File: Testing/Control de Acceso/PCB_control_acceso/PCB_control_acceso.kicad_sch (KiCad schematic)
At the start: 26 parts, among them J1 Doorstat, J2 PROG, J3 IN 5V, J4 Screw_Terminal_01x03, J5 Screw_Terminal_01x03, K1 Relay_DPDT, Q1 NMOS, SW1 SW_MEC_5G, U1 ESP-12F, U2 LM1117DT-3.3

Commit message: pcb control acceso
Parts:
- removed D1: D, symbol Device:D
- removed D2: LED_Small, symbol Device:LED_Small
- removed Q1: NMOS, Package_TO_SOT_SMD:SOT-23, symbol Simulation_SPICE:NMOS
- removed R5: 10K, Resistor_SMD:R_0805_2012Metric, symbol Device:R
- added D1: LED, LED_THT:LED_D3.0mm, symbol Device:LED
- added D3: 1N4148, Diode_THT:D_DO-35_SOD27_P7.62mm_Horizontal, symbol Diode:1N4148
- added Q1: BC546, Package_TO_SOT_THT:TO-92_Inline, symbol Transistor_BJT:BC546
- C1, C2: footprint Capacitor_SMD:C_0805_2012Metric -> Capacitor_THT:C_Disc_D3.0mm_W2.0mm_P2.50mm
- C3, C4: footprint (none) -> Capacitor_THT:CP_Radial_D5.0mm_P2.50mm
- J2: footprint (none) -> Connector_PinHeader_1.27mm:PinHeader_1x04_P1.27mm_Vertical
- R8: value 1K -> 10K
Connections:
- net +5V: now also D3.1 (K)
- net GND: now also Q1.3 (E)
- net at K1.A2: now also D1.1 (K), D3.2 (A), Q1.1 (C)
- net at R10.1: now also D1.2 (A)
- net at R8.2, R9.1: now also Q1.2 (B)

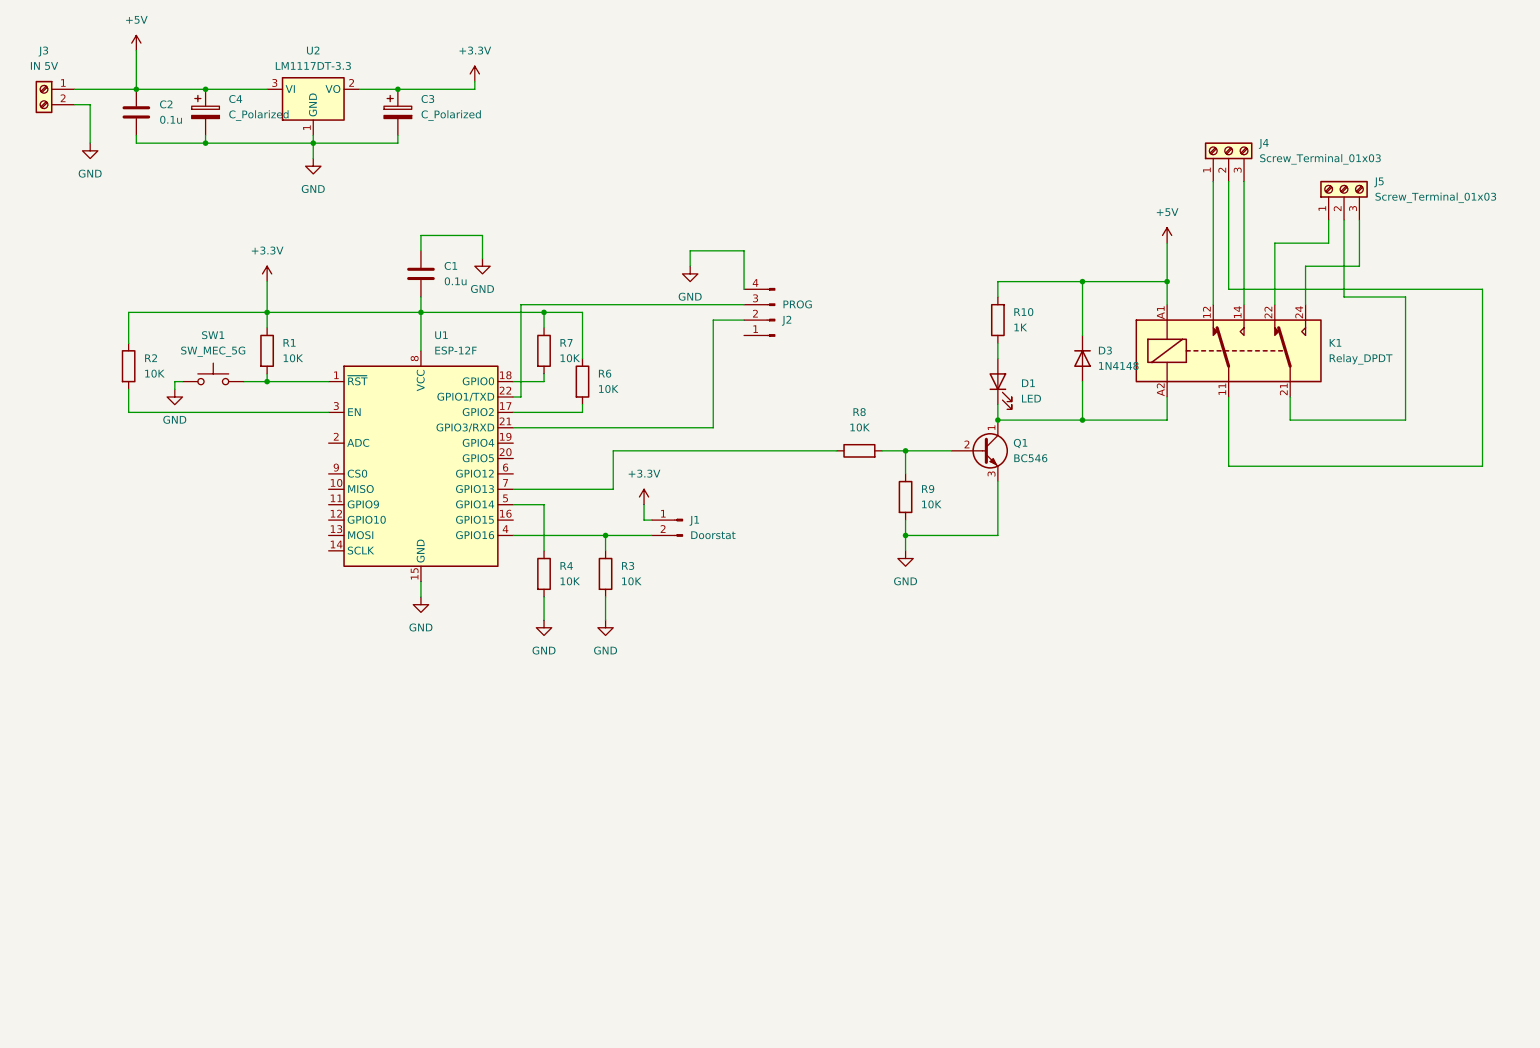
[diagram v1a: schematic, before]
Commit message: pcb control acceso
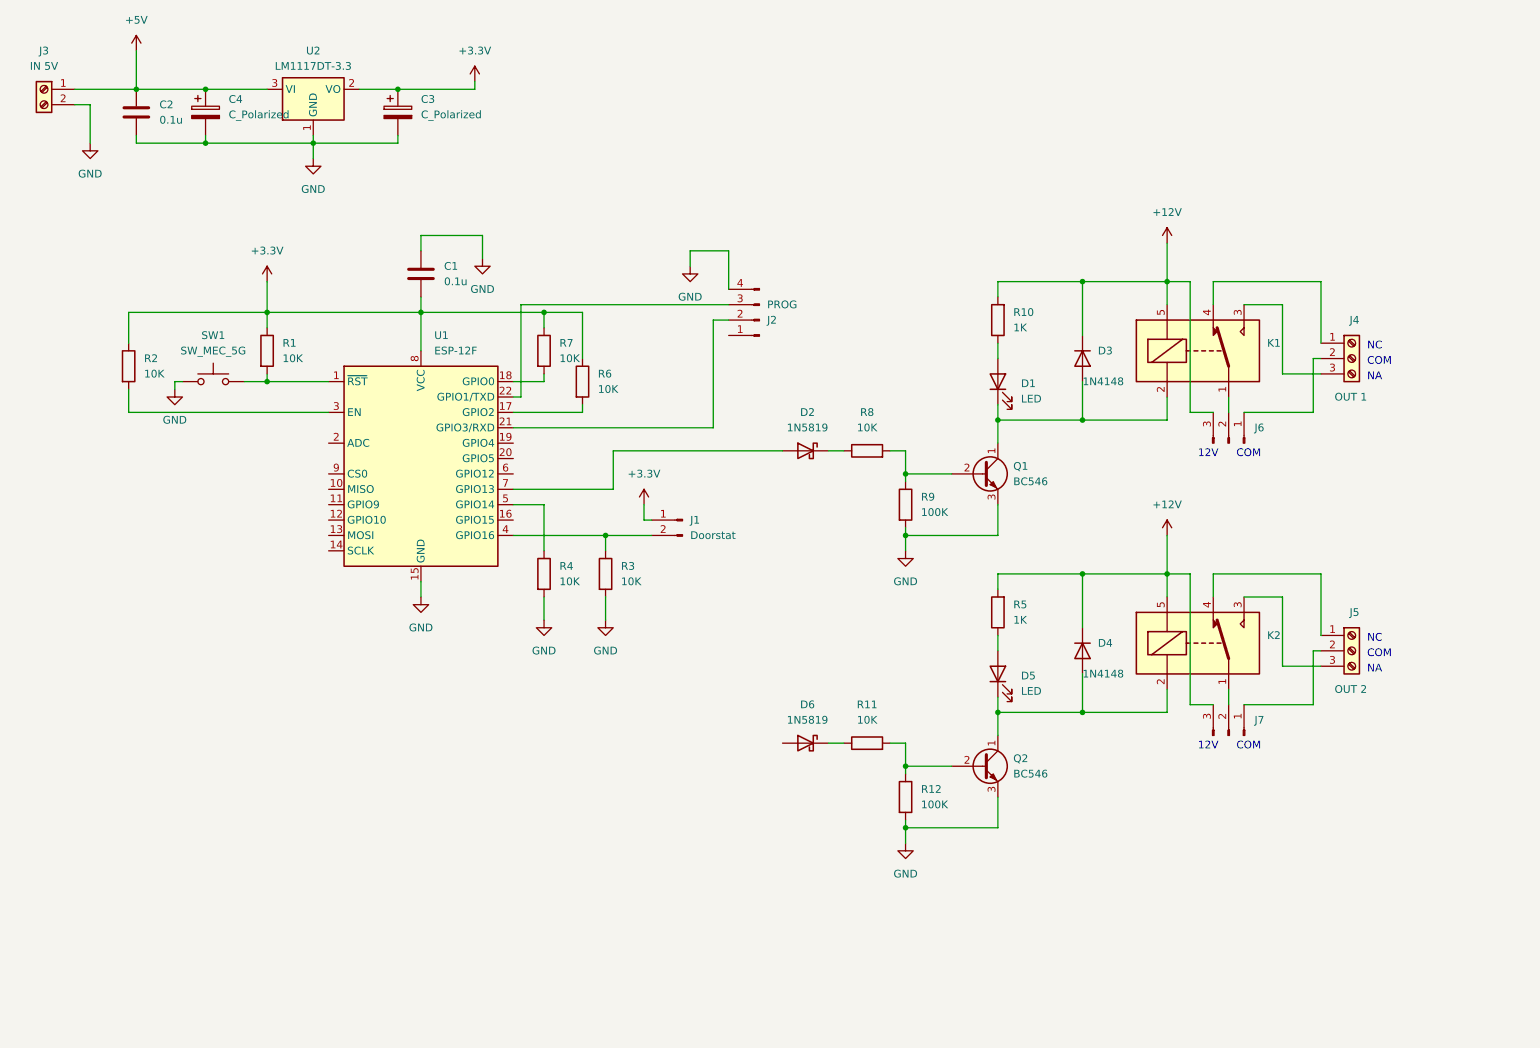
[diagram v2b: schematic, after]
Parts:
- removed K1: Relay_DPDT, Relay_THT:Relay_DPDT_Finder_30.22, symbol Relay:Relay_DPDT
- added D2, D6: 1N5819, Diode_THT:D_DO-41_SOD81_P10.16mm_Horizontal, symbol Diode:1N5819
- added D4: 1N4148, Diode_THT:D_DO-35_SOD27_P7.62mm_Horizontal, symbol Diode:1N4148
- added D5: LED, LED_THT:LED_D3.0mm, symbol Device:LED
- added J6, J7: ~, symbol Connector:Conn_01x03_Pin
- added K1, K2: SANYOU_SRD_Form_C, Relay_THT:Relay_SPDT_SANYOU_SRD_Series_Form_C, symbol Relay:SANYOU_SRD_Form_C
- added Q2: BC546, Package_TO_SOT_THT:TO-92_Inline, symbol Transistor_BJT:BC546
- added R11: 10K, Resistor_SMD:R_0805_2012Metric, symbol Device:R
- added R12: 100K, Resistor_SMD:R_0805_2012Metric, symbol Device:R
- added R5: 1K, Resistor_SMD:R_0805_2012Metric, symbol Device:R
- J4: value Screw_Terminal_01x03 -> OUT 1
- J5: value Screw_Terminal_01x03 -> OUT 2
- R9: value 10K -> 100K
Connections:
- net +5V: no longer D3.1 (K), R10.2
- net GND: now also Q2.3 (E), R12.2
- net at U1.7 (GPIO13): now also D2.2 (A); no longer R8.1
- net at J5.1 (Pin_1): now also K2.4
- net at J5.2 (Pin_2): now also J7.1 (Pin_1)
- net at J5.3 (Pin_3): now also K2.3
- net at J4.1 (Pin_1): now also K1.4
- net at J4.2 (Pin_2): now also J6.1 (Pin_1)
- net at J4.3 (Pin_3): now also K1.3
- net at D1.1 (K), D3.2 (A), Q1.1 (C): now also K1.2
- new net: D4.2 (A), D5.1 (K), K2.2, Q2.1 (C)
- new net: D5.2 (A), R5.1
- new net: D6.1 (K), R11.1
- new net: Q2.2 (B), R11.2, R12.1
- new net: J7.2 (Pin_2), K2.1
- new net: J6.2 (Pin_2), K1.1
- new net: D2.1 (K), R8.1
- new net +12V: D3.1 (K), D4.1 (K), J6.3 (Pin_3), J7.3 (Pin_3), K1.5, K2.5, R10.2, R5.2
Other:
- note added: "12V"
- note added: "COM"
- note added: "NA"
- note added: "NC"
- moved on the sheet: J2, Q1, R8, R9

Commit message: actualizacion 27/7/24
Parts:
- removed D2, D6: 1N5819, Diode_THT:D_DO-41_SOD81_P10.16mm_Horizontal, symbol Diode:1N5819
- removed D5: LED, LED_THT:LED_D3.0mm, symbol Device:LED
- removed J1: Doorstat, Connector_PinHeader_1.27mm:PinHeader_1x02_P1.27mm_Vertical, symbol Connector:Conn_01x02_Pin
- removed J2: PROG, Connector_PinHeader_1.27mm:PinHeader_1x04_P1.27mm_Vertical, symbol Connector:Conn_01x04_Pin
- removed J5: OUT 2, symbol Connector:Screw_Terminal_01x03
- removed K2: SANYOU_SRD_Form_C, Relay_THT:Relay_SPDT_SANYOU_SRD_Series_Form_C, symbol Relay:SANYOU_SRD_Form_C
- removed Q2: BC546, Package_TO_SOT_THT:TO-92_Inline, symbol Transistor_BJT:BC546
- removed SW1: SW_MEC_5G, symbol Switch:SW_MEC_5G
- removed U2: LM1117DT-3.3, Package_TO_SOT_SMD:TO-252-3_TabPin2, symbol Regulator_Linear:LM1117DT-3.3
- added C5: 0.1u, Capacitor_THT:C_Disc_D3.0mm_W2.0mm_P2.50mm, symbol Device:C
- added D2, D5: 1N4148, Diode_THT:D_DO-35_SOD27_P5.08mm_Vertical_KathodeUp, symbol Diode:1N4148
- added J1: LECTOR, TerminalBlock_Phoenix:TerminalBlock_Phoenix_MKDS-1,5-6-5.08_1x06_P5.08mm_Horizontal, symbol Connector:Screw_Terminal_01x06
- added J10: ESP01, Connector_PinSocket_2.54mm:PinSocket_2x04_P2.54mm_Vertical, symbol Connector_Generic:Conn_02x04_Counter_Clockwise
- added J11: Receptor RF, Connector_PinHeader_2.54mm:PinHeader_1x04_P2.54mm_Vertical, symbol Connector:Conn_01x04_Pin
- added J12, J14, J15, J17, J2, J21, J8, J9: ~, Connector_PinHeader_1.27mm:PinHeader_1x01_P1.27mm_Vertical, symbol Connector:Conn_01x01_Pin
- added J13: OUT 1, TerminalBlock_Phoenix:TerminalBlock_Phoenix_MKDS-1,5-3_1x03_P5.00mm_Horizontal, symbol Connector:Screw_Terminal_01x03
- added J16, J18, J22: ~, Connector_PinHeader_2.54mm:PinHeader_1x01_P2.54mm_Vertical, symbol Connector:Conn_01x01_Pin
- added J5: IN 12V, TerminalBlock_Phoenix:TerminalBlock_Phoenix_MKDS-1,5-2_1x02_P5.00mm_Horizontal, symbol Connector:Screw_Terminal_01x02
- added R13: 10K, Resistor_THT:R_Axial_DIN0309_L9.0mm_D3.2mm_P2.54mm_Vertical, symbol Device:R
- added R16: 10K, Resistor_THT:R_Axial_DIN0207_L6.3mm_D2.5mm_P7.62mm_Horizontal, symbol Device:R
- added SW1: FLASH, Button_Switch_THT:SW_PUSH_1P1T_6x3.5mm_H4.3_APEM_MJTP1243, symbol Switch:SW_Omron_B3FS
- added SW4: RESET, Button_Switch_THT:SW_PUSH_1P1T_6x3.5mm_H4.3_APEM_MJTP1243, symbol Switch:SW_Omron_B3FS
- added U3: AMS1117-3.3, Package_TO_SOT_SMD:SOT-223-3_TabPin2, symbol Regulator_Linear:AMS1117-3.3
- C3: value C_Polarized -> 10uF
- C4: value C_Polarized -> 100uF
- D3, D4: footprint Diode_THT:D_DO-35_SOD27_P7.62mm_Horizontal -> Diode_THT:D_DO-35_SOD27_P5.08mm_Vertical_KathodeUp
- J3: footprint (none) -> TerminalBlock_Phoenix:TerminalBlock_Phoenix_MKDS-1,5-2_1x02_P5.00mm_Horizontal
- J4: footprint (none) -> TerminalBlock_Phoenix:TerminalBlock_Phoenix_MKDS-1,5-3_1x03_P5.00mm_Horizontal
- J6: footprint (none) -> Connector_PinHeader_2.54mm:PinHeader_1x03_P2.54mm_Vertical
- J7: value ~ -> PROG; footprint (none) -> Connector_PinHeader_2.54mm:PinHeader_1x03_P2.54mm_Vertical
- R1, R10, R2: footprint Resistor_SMD:R_0805_2012Metric -> Resistor_THT:R_Axial_DIN0309_L9.0mm_D3.2mm_P2.54mm_Vertical
- R11, R3, R4, R6, R7, R8, R9: footprint Resistor_SMD:R_0805_2012Metric -> Resistor_THT:R_Axial_DIN0207_L6.3mm_D2.5mm_P7.62mm_Horizontal
- R12: value 100K -> 10K; footprint Resistor_SMD:R_0805_2012Metric -> Resistor_THT:R_Axial_DIN0207_L6.3mm_D2.5mm_P7.62mm_Horizontal
- R5: value 1K -> 10K; footprint Resistor_SMD:R_0805_2012Metric -> Resistor_THT:R_Axial_DIN0207_L6.3mm_D2.5mm_P7.62mm_Horizontal
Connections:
- net +12V: now also J1.6 (Pin_6), J5.2 (Pin_2); no longer D4.1 (K), J7.3 (Pin_3), R5.2
- net +3.3V: now also R6.2, J10.8 (Pin_8), J12.1 (Pin_1), J13.1 (Pin_1), J18.1 (Pin_1), R16.1, U3.2 (VO); no longer R6.1
- net +5V: now also J3.2 (Pin_2), C5.2, J11.4 (Pin_4), J16.1 (Pin_1), J22.1 (Pin_1), U3.3 (VI); no longer J3.1 (Pin_1)
- net GND: now also J3.1 (Pin_1), J7.1 (Pin_1), R11.2, C5.1, J1.5 (Pin_5), J10.1 (Pin_1), J11.1 (Pin_1), J5.1 (Pin_1), SW1.2, SW4.1, U3.1 (GND); no longer J3.2 (Pin_2), R12.2
- net at D4.2 (A): now also U1.7 (GPIO13)
- net at R5.1: now also J1.2 (Pin_2)
- net at R3.1, U1.4 (GPIO16): now also J13.3 (Pin_3)
- net LED: now reaches R11.1
- net LED: now also U1.16 (GPIO15), J1.1 (Pin_1), J14.1 (Pin_1), J9.1 (Pin_1)
- net D1: now reaches R12.1
- net D1: now also U1.20 (GPIO5), D2.2 (A); no longer R11.2
- net at J7.2 (Pin_2): now also U1.21 (GPIO3/RXD)
- net at R1.2, U1.1 (~{RST}): now also J15.1 (Pin_1), SW4.2
- net GPIO2: now reaches U1.17 (GPIO2)
- net GPIO2: now also R6.1, J2.1 (Pin_1); no longer R6.2
- net WG26/34: now reaches R7.2, U1.18 (GPIO0)
- net WG26/34: now also J21.1 (Pin_1), SW1.1
- net D0: now reaches U1.19 (GPIO4)
- net D0: now also D5.2 (A), R13.2
- net at U1.22 (GPIO1/TXD): now also J7.3 (Pin_3)
- net BTN: now reaches R4.1, U1.5 (GPIO14)
- net BTN: now also J13.2 (Pin_2)
- net BEEP: now reaches U1.6 (GPIO12)
- net BEEP: now also R5.2
- net at R8.1: now also D4.1 (K)
- net at J4.1 (Pin_1): now also K1.3; no longer K1.4
- net at J4.3 (Pin_3): now also K1.4; no longer K1.3
- new net: J10.4 (Pin_4), R16.2
- new net: J10.7 (Pin_7), J11.2 (Pin_2)
- new net: D2.1 (K), J1.4 (Pin_4)
- new net: J10.6 (Pin_6), J8.1 (Pin_1)
- new net: J10.2 (Pin_2), J17.1 (Pin_1)
- new net: J10.3 (Pin_3), R13.1
- new net: J10.5 (Pin_5), R12.2
- new net: D5.1 (K), J1.3 (Pin_3)
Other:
- note added: "3V3"
- note added: "BTN"
- note added: "DOORSTAT"
- moved on the sheet: R3
